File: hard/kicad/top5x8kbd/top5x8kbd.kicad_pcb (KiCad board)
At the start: 2 copper layers, 177.8 x 130.8 mm, 79 parts, among them J1 IOx, J16 COLUMN, J17 ROW, J2 IOx, J23 MD/VCS1, J44 MD/VCS2, J5 TO COMPUTER, SW1 1 !, SW10 0 _, SW11 Q ¡, SW12 W ~~, SW13 E é, SW14 R <, SW15 T >, SW16 Y ü, SW17 U ú, SW18 I í, SW19 O ó, SW2 2 @, SW20 P ", SW21 A á, SW22 S ;, SW23 D |, SW24 F [, SW25 G ], SW26 H ^, SW27 J -, SW28 K +, SW29 L =, SW3 3 #, SW30 ENTER ñ, SW31 SHIFT, SW32 Z :, SW33 X ¿, SW34 C ?, SW35 V /, SW36 B *, SW37 N ,, SW38 M ., SW39 ALT, SW4 4 $, SW40 SPACE, SW5 5 %, SW6 6 &, SW7 7 ', SW8 8 (, SW9 9 (, U1 74HC138, U12 74HC174, U13 74HC245, U24 74HC245, U26 74HC174, U34 74HC595, U45 74HC245, U55 74HC595, U9 74HC86

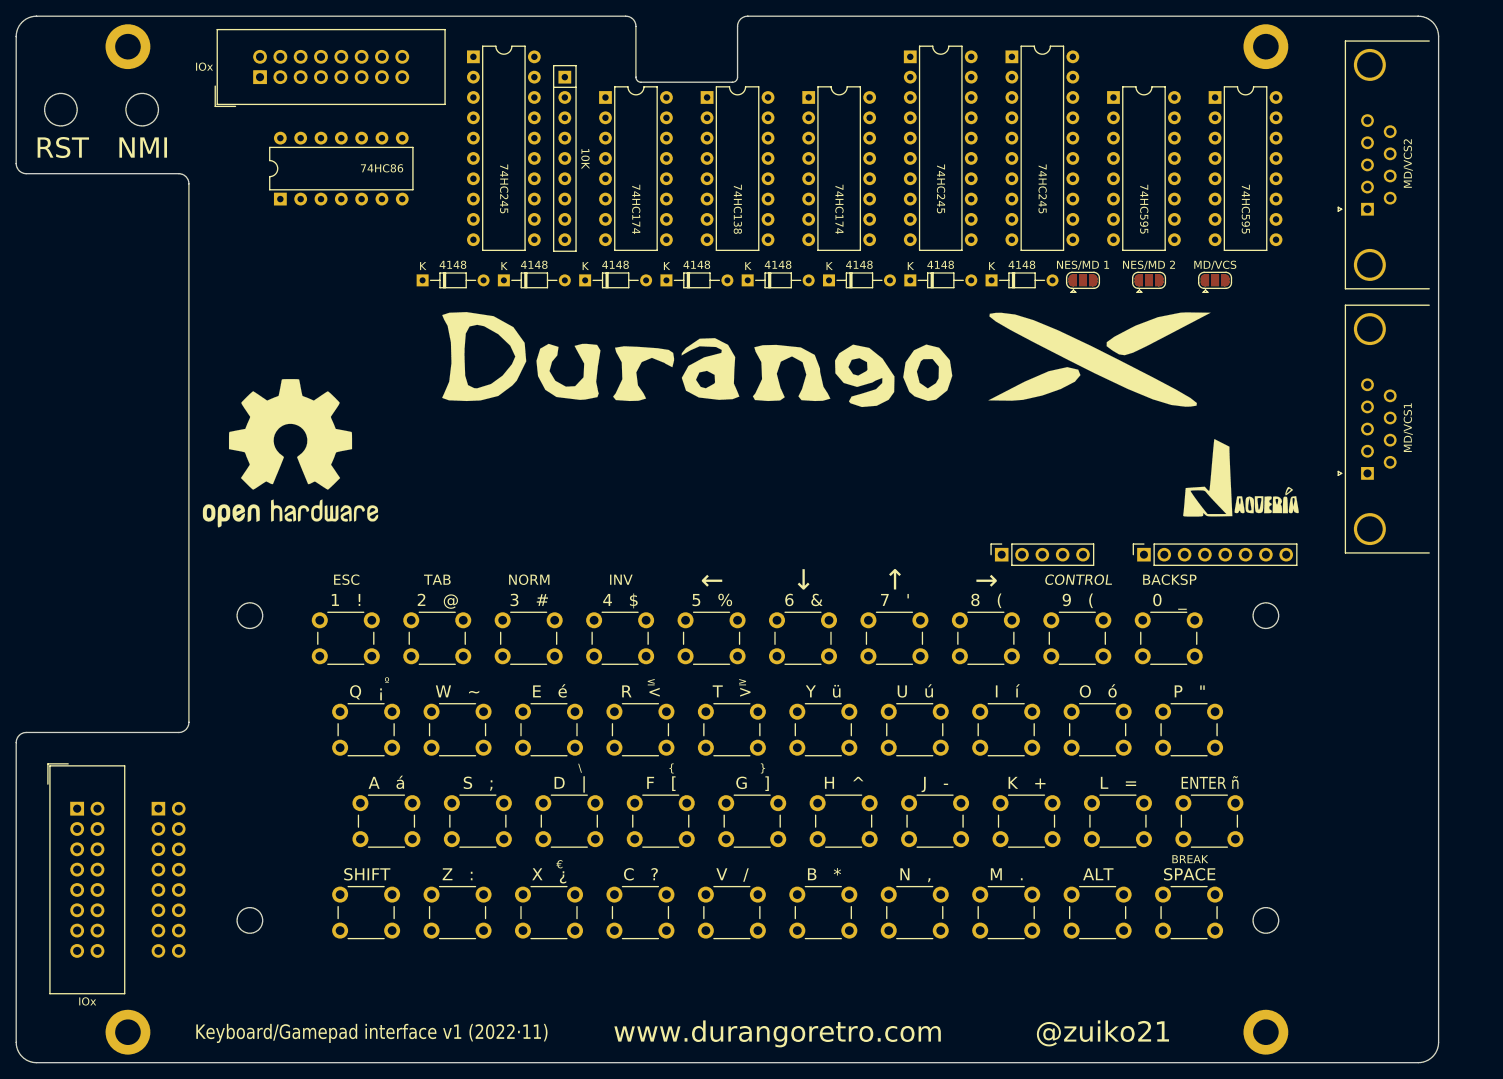
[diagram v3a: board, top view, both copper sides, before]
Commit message: add holes for LEDs
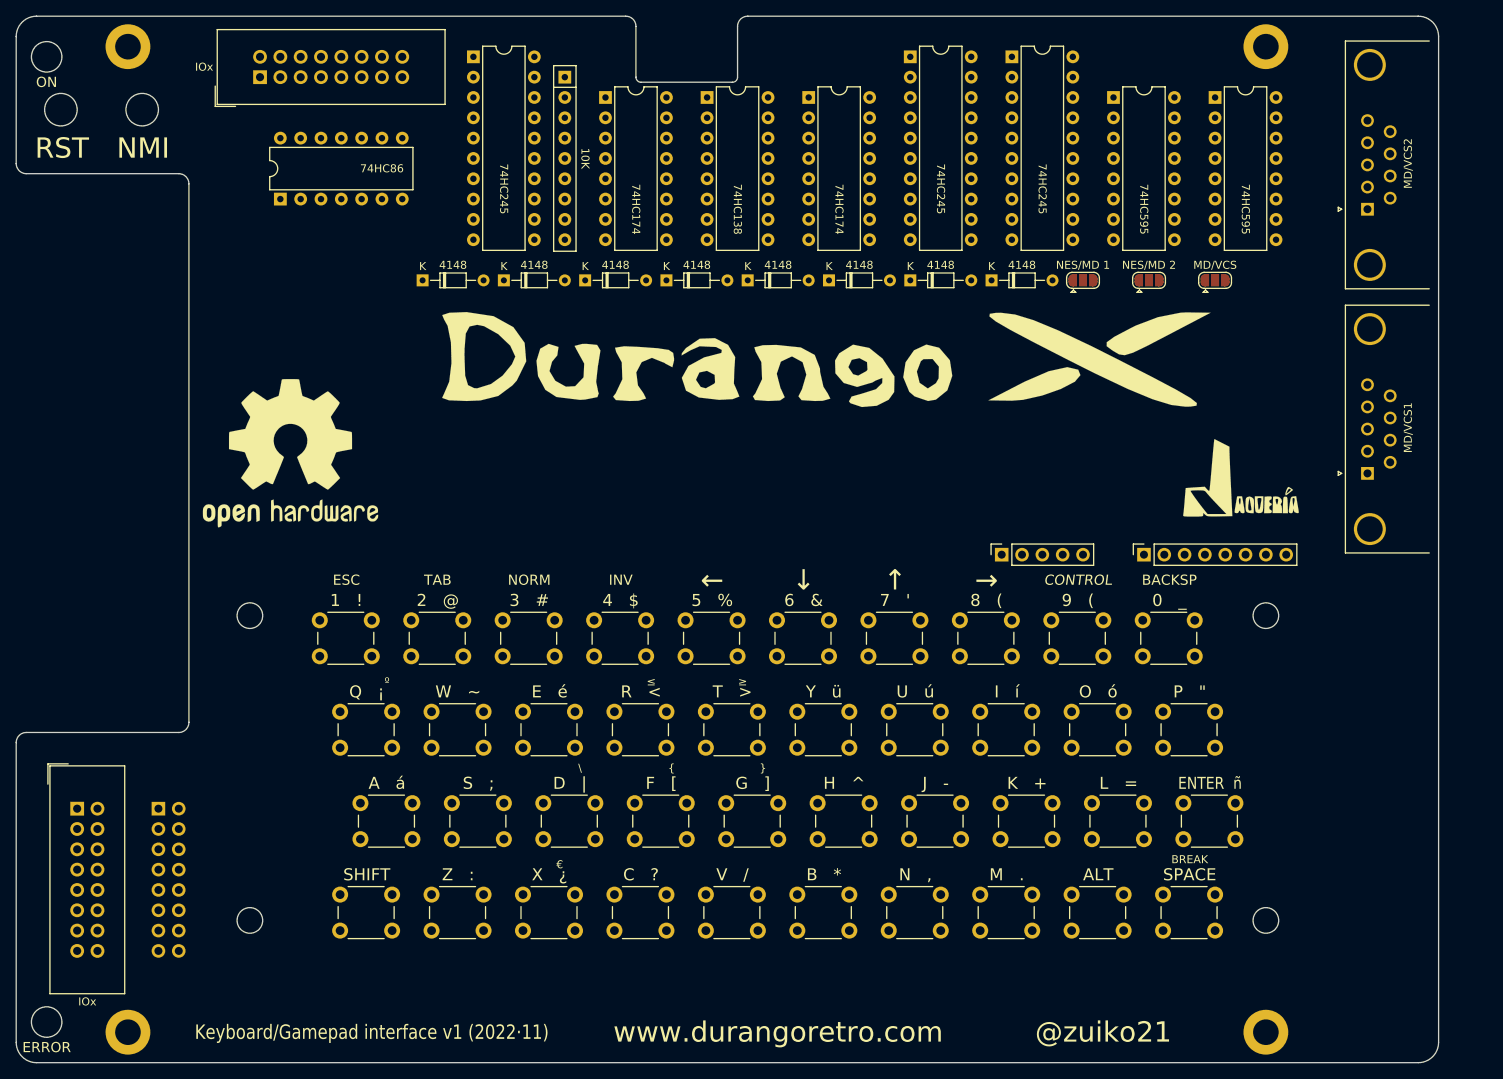
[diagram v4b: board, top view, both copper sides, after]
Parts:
- SW30: value ENTER ñ -> ENTER ñ
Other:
- outline, holes or cut-outs redrawn
- board text added: "ERROR"
- board text added: "ON"
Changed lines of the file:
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@@
   (general
     (thickness 1.6)
-    (drawings 29)
+    (drawings 33)
     (tracks 0)
     (zones 0)
@@
       (effects (font (size 1 1) (thickness 0.15)) (justify mirror))
     )
-    (fp_text value "ENTER ñ" (at 3.175 6.985) (layer F.SilkS)
+    (fp_text value "ENTER  ñ" (at 3.175 6.985) (layer F.SilkS)
       (effects (font (size 1.5 1.27) (thickness 0.2)))
     )
@@
     )
   )
+  (gr_text ERROR (at 16.51 141.605) (layer F.SilkS)
+    (effects (font (size 1.27 1.27) (thickness 0.254)))
+  )
+  (gr_text ON (at 16.51 20.955) (layer F.SilkS)
+    (effects (font (size 1.27 1.27) (thickness 0.254)))
+  )
+  (gr_circle (center 16.51 138.43) (end 18.415 138.43) (layer Edge.Cuts) (width 0.12))
+  (gr_circle (center 16.51 17.78) (end 18.415 17.78) (layer Edge.Cuts) (width 0.12))
   (gr_arc (start 102.235 20.32) (end 102.235 20.955) (angle -90) (layer Edge.Cuts) (width 0.05))
   (gr_arc (start 90.805 20.32) (end 90.17 20.32) (angle -90) (layer Edge.Cuts) (width 0.05))

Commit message: complete 5x8 schematic
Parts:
- removed JP1: NES/MD 1, Jumper:SolderJumper-3_P1.3mm_Open_RoundedPad1.0x1.5mm
- removed JP2: NES/MD 2, Jumper:SolderJumper-3_P1.3mm_Open_RoundedPad1.0x1.5mm
- added D19: PASK, LED_THT:LED_D3.0mm, F.Cu at (116.8, 17.8)
- added R11: 560, Resistor_THT:R_Axial_DIN0207_L6.3mm_D2.5mm_P10.16mm_Horizontal, F.Cu at (124.5, 45.7)
- added RN22: 220K, Resistor_THT:R_Array_SIP9, F.Cu at (132.1, 17.8)
- added RN43: 220K, Resistor_THT:R_Array_SIP9, F.Cu at (147.3, 17.8)
- U1, U12, U26, U34, U55: footprint Package_DIP:DIP-16_W7.62mm -> Package_DIP:DIP-16_W7.62mm_Socket
- U13, U24, U45: footprint Package_DIP:DIP-20_W7.62mm -> Package_DIP:DIP-20_W7.62mm_Socket
- U9: footprint Package_DIP:DIP-14_W7.62mm -> Package_DIP:DIP-14_W7.62mm_Socket
- moved LOGO3 121.0 mm to (47.0, 47.0)
- moved JP21 60.2 mm to (109.2, 17.8)
- moved U24 16.5 mm to (120.7, 17.8)
- moved D16 12.7 mm to (127.0, 45.7)
- moved D17 12.7 mm to (137.2, 45.7)
- moved D18 12.7 mm to (147.3, 45.7)
- moved U55 12.7 mm to (162.6, 22.9)
- moved U34 11.4 mm to (151.1, 22.9)
- moved U45 11.4 mm to (135.9, 17.8)
- moved J16 10.2 mm to (135.9, 69.8)
- moved J17 10.2 mm to (153.7, 69.8)
- moved U26 2.54 mm to (109.2, 22.9)
- moved LOGO2 1.91 mm to (115.6, 57.1)
- moved U13 1.27 mm to (71.1, 17.8)
- moved RN11 1.27 mm to (82.5, 20.3)
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- renumbered JP23 to JP21
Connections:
- J23 pad 1: (no net) -> /~UP1
- J23 pad 2: (no net) -> /~DN1
- J23 pad 3: (no net) -> /~LT1
- J23 pad 4: (no net) -> /~RT1
- J23 pad 5: (no net) -> +5V
- J23 pad 6: (no net) -> /~AB1
- J23 pad 7: (no net) -> /LATCH
- J23 pad 8: (no net) -> GND
- J23 pad 9: (no net) -> /~SC1
- J44 pad 1: (no net) -> /~UP2
- J44 pad 2: (no net) -> /~DN2
- J44 pad 3: (no net) -> /~LT2
- J44 pad 4: (no net) -> /~RT2
- J44 pad 5: (no net) -> +5V
- J44 pad 6: (no net) -> /~AB2
- J44 pad 7: (no net) -> /LATCH
- J44 pad 8: (no net) -> GND
- J44 pad 9: (no net) -> /~SC2
- SW38 pad 1: Net-(SW38-Pad1) -> COL3
- U1 pad 14: (no net) -> /~ERR
- U24 pad 11: (no net) -> /~B1
- U24 pad 12: (no net) -> /~SC1
- U24 pad 13: (no net) -> /~AB1
- U24 pad 14: (no net) -> /~C1
- U24 pad 15: (no net) -> /~UP1
- U24 pad 16: (no net) -> /~LT1
- U24 pad 17: (no net) -> /~DN1
- U24 pad 18: (no net) -> /~RT1
- U24 pad 19: /M1~OE -> /P1~OE
- U26 pad 10: (no net) -> /~B2
- U26 pad 11: (no net) -> /~AB2
- U26 pad 12: (no net) -> /~C2
- U26 pad 13: (no net) -> /~SC2
- U26 pad 14: (no net) -> +5V
- U26 pad 3: (no net) -> +5V
- U26 pad 4: (no net) -> /~SC1
- U26 pad 5: (no net) -> /~C1
- U26 pad 6: (no net) -> /~AB1
- U26 pad 7: (no net) -> /~B1
- U34 pad 1: PD1 -> PD2
- U34 pad 11: (no net) -> /NCLK
- U34 pad 12: (no net) -> /~NCLK
- U34 pad 13: /N1~OE -> /P1~OE
- U34 pad 14: (no net) -> /~DAT1
- U34 pad 2: PD2 -> PD1
- U34 pad 4: PD4 -> PD6
- U34 pad 5: PD5 -> PD4
- U34 pad 6: PD6 -> PD5
- U45 pad 11: (no net) -> /~B2
- U45 pad 12: (no net) -> /~SC2
- U45 pad 13: (no net) -> /~AB2
- U45 pad 14: (no net) -> /~C2
- U45 pad 15: (no net) -> /~UP2
- U45 pad 16: (no net) -> /~LT2
- U45 pad 17: (no net) -> /~DN2
- U45 pad 18: (no net) -> /~RT2
- U45 pad 19: /M2~OE -> /P2~OE
- U55 pad 1: PD1 -> PD2
- U55 pad 11: (no net) -> /NCLK
- U55 pad 12: (no net) -> /~NCLK
- U55 pad 13: /N2~OE -> /P2~OE
- U55 pad 14: (no net) -> /~DAT2
- U55 pad 2: PD2 -> PD1
- U55 pad 4: PD4 -> PD6
- U55 pad 5: PD5 -> PD4
- U55 pad 6: PD6 -> PD5
- U9 pad 11: (no net) -> /LATCH
- U9 pad 8: (no net) -> /NCLK
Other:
- outline, holes or cut-outs redrawn

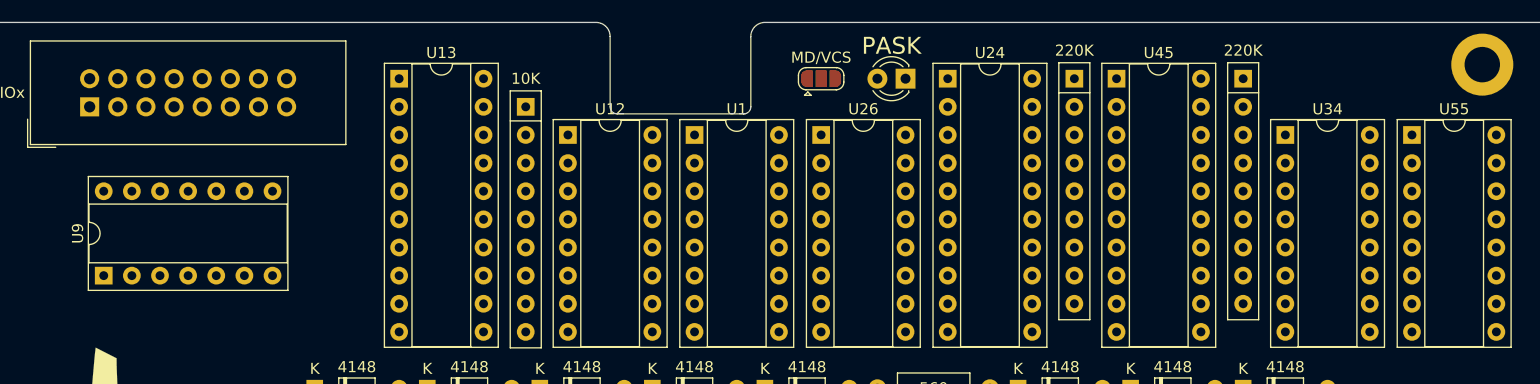
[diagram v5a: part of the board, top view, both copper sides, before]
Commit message: fix silkscreen, missing NES conn schematic
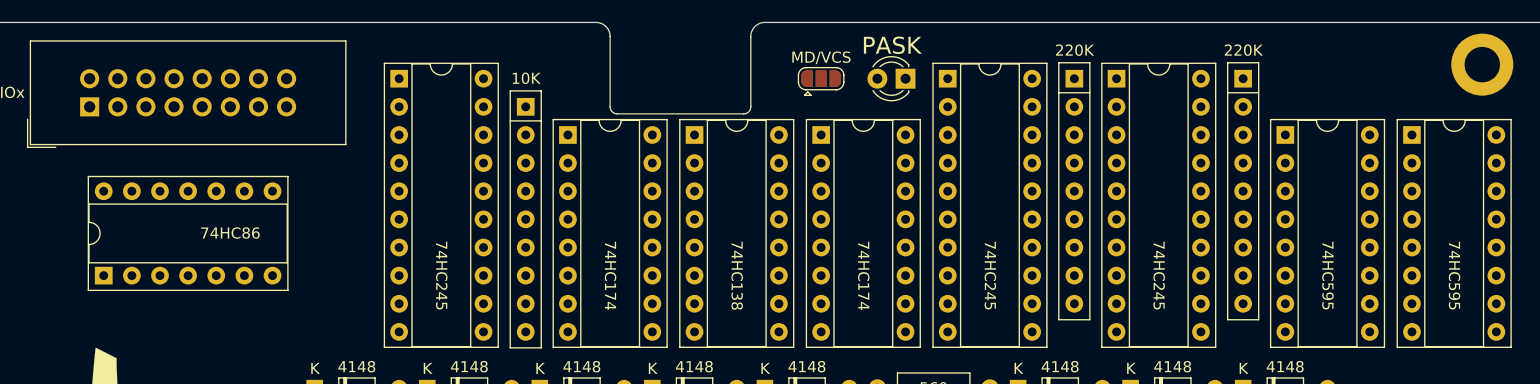
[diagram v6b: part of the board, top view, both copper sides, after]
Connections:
- U1 pad 9: /~CLOCK -> /~NCLK
- U9 pad 9: /~CLOCK -> /~NCLK

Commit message: makeshift NES connector placement
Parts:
- added J33: NES 1, Connector_PinHeader_2.54mm:PinHeader_2x04_P2.54mm_Horizontal, F.Cu at (176.5, 61.0)
- added J54: NES 2, Connector_PinHeader_2.54mm:PinHeader_2x04_P2.54mm_Horizontal, F.Cu at (176.5, 27.9)

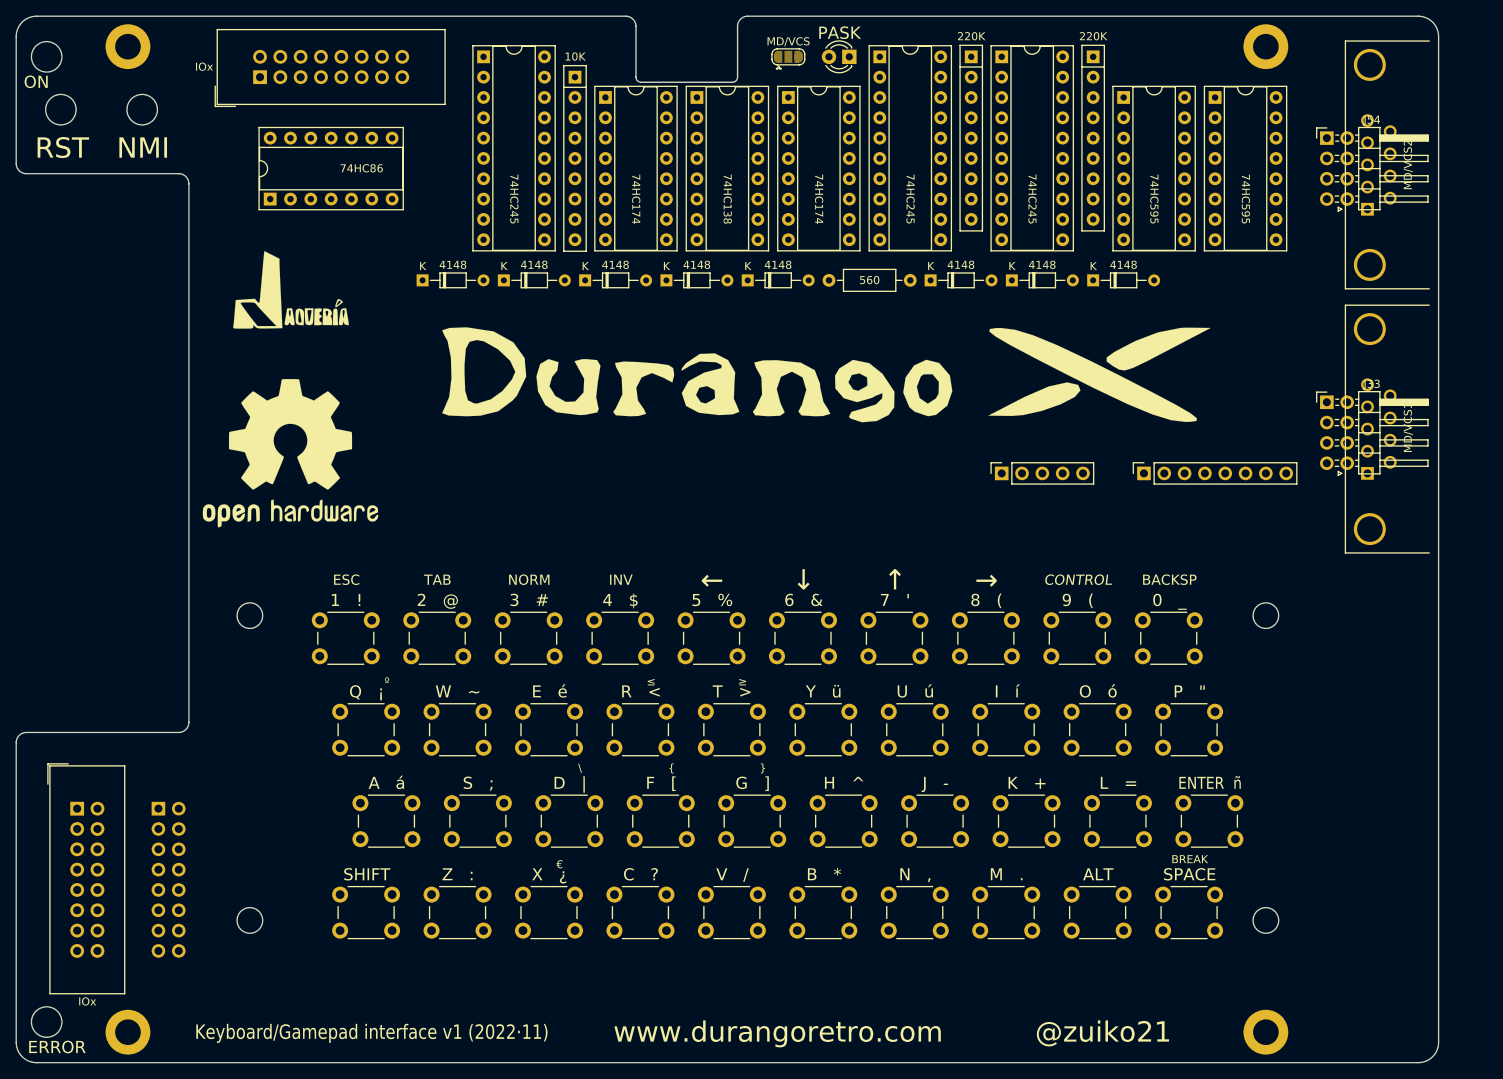
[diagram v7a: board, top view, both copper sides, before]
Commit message: NES footprint on elongated cover keyboard
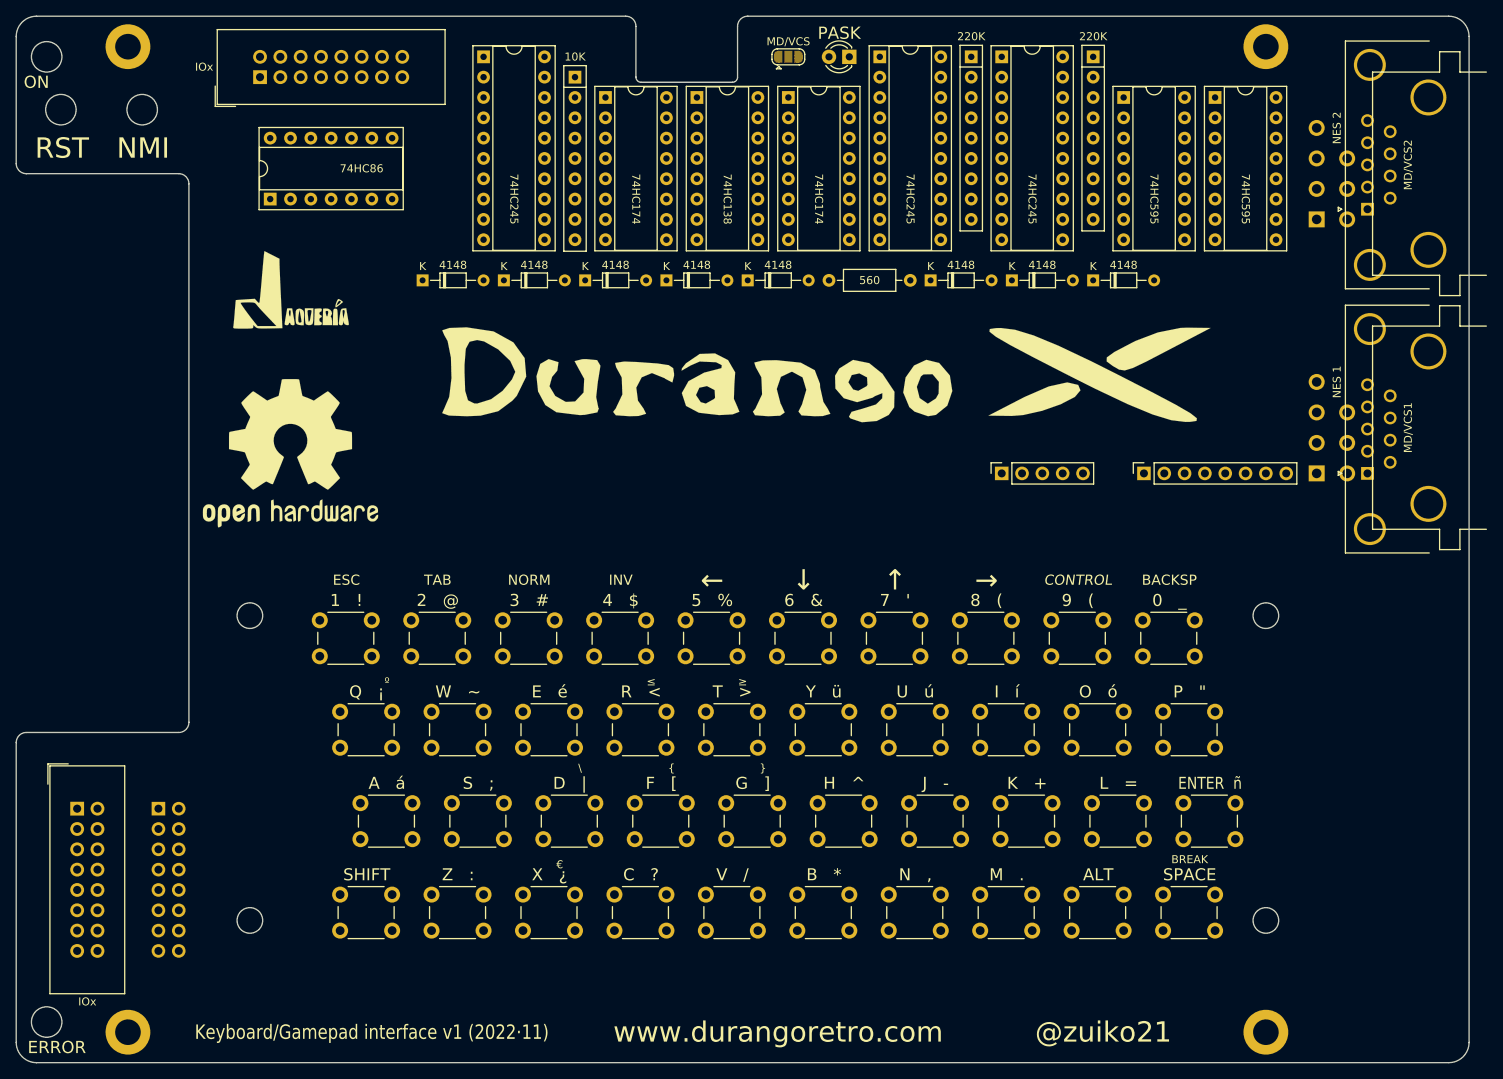
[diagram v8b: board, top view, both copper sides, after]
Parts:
- J33, J54: footprint Connector_PinHeader_2.54mm:PinHeader_2x04_P2.54mm_Horizontal -> durango:NES gamepad
- moved J54 10.2 mm to (175.3, 38.1), turned to 90 degrees
- moved J33 8.98 mm to (175.3, 69.8), turned to 90 degrees
- renumbered RN43 to RN3
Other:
- board size 177.8 x 130.8 mm -> 181.6 x 130.8 mm
